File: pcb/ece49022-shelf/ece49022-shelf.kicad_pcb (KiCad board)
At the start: 4 copper layers, 44.2 x 53.6 mm, 69 parts, among them IC1 NAU7802, J1 USB_B_Micro, J2 Conn_01x16_Pin, J3 Conn_01x04_Pin, J4 SM03B-SRSS-TB, J6 Conn_01x02_Pin, J7 Conn_01x02_Pin, SW1 SW_Push, SW2 SW_Push, U2 TPS54202DDCT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

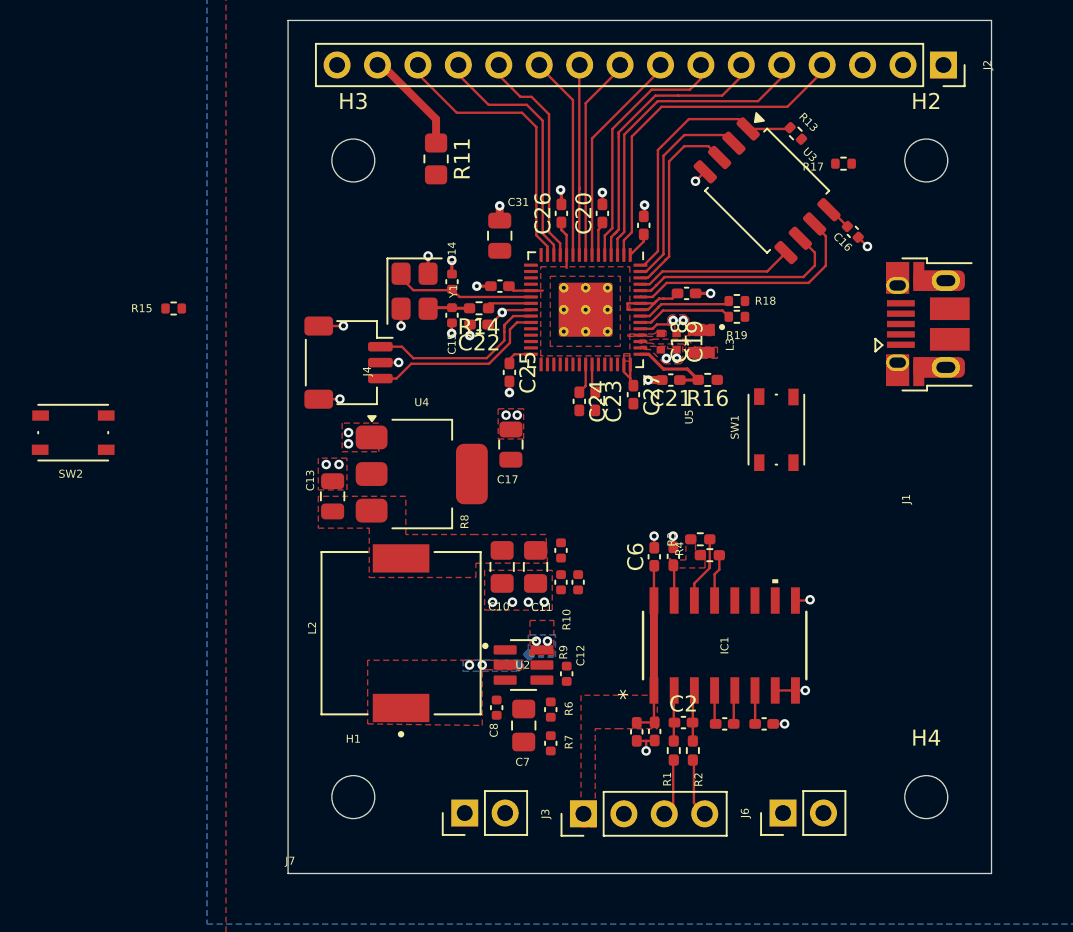
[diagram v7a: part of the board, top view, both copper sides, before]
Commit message: edited nau7802 schem and changed pins for layout reasons
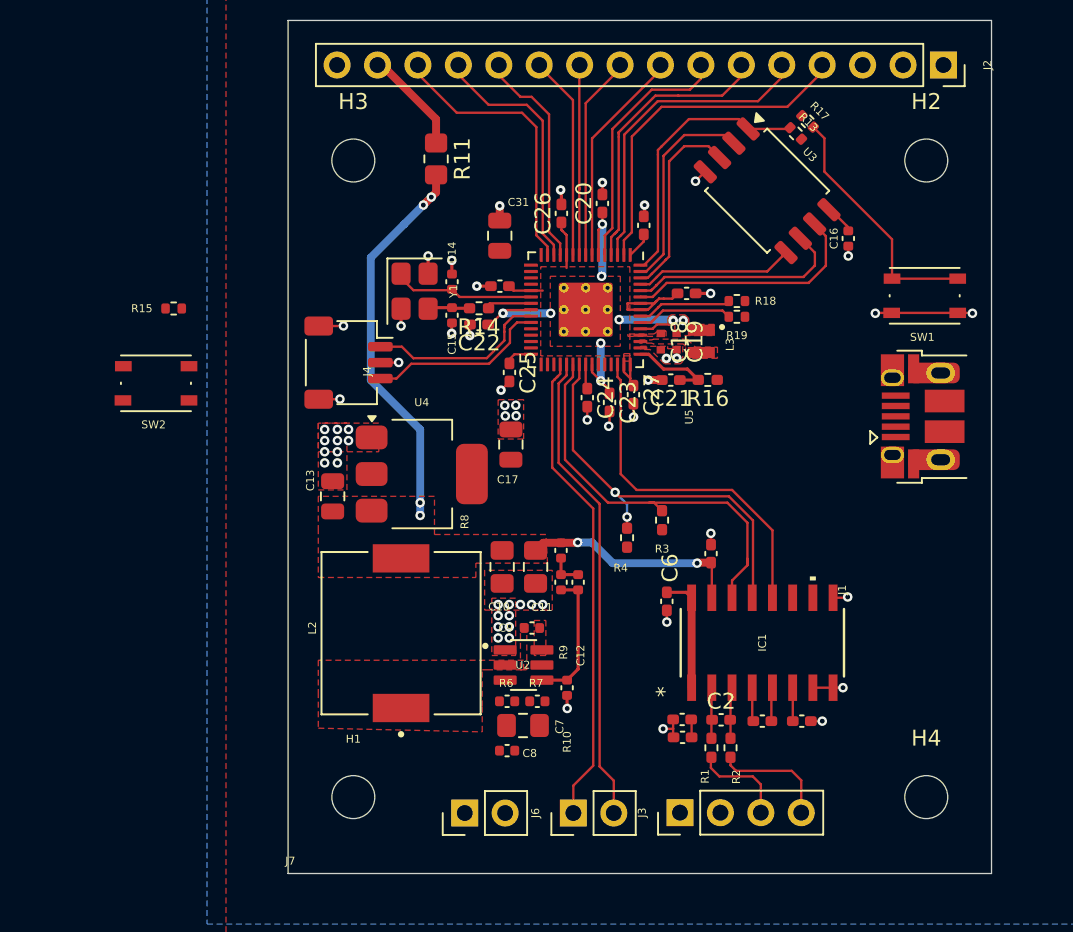
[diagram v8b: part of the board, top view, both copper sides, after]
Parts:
- C9: moved to F.Cu
- moved J6 13.2 mm to (171.8, 112.0)
- moved SW1 12.6 mm to (193.9, 79.5), turned to 180 degrees
- moved J3 6.07 mm to (178.5, 112.0)
- moved SW2 6.05 mm to (145.6, 85.0)
- moved J1 5.81 mm to (194.9, 87.1)
- moved R4 5.32 mm to (175.2, 94.7), turned to -90 degrees
- moved R17 3.49 mm to (186.5, 68.5), turned to -45 degrees
- moved C4 2.96 mm to (178.7, 106.1), turned to 180 degrees
- moved C6 2.91 mm to (177.7, 98.7), turned to -90 degrees
- moved R6 2.79 mm to (167.7, 105.0), turned to 0 degrees
- moved C8 2.78 mm to (167.7, 108.1), turned to 0 degrees
- moved R7 2.77 mm to (169.6, 105.0), turned to 0 degrees
- moved R3 2.68 mm to (177.4, 93.6), turned to -90 degrees
- moved C2 2.37 mm to (181.1, 106.1)
- moved C5 2.37 mm to (186.2, 106.2)
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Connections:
- R3 pad 2: +5V -> +3V3
- R4 pad 2: +5V -> +3V3
- U5 pad 15: /LOAD_CELL_I2C_SDA -> /RP2350A/GPIO11
- U5 pad 16: /LOAD_CELL_I2C_SCL -> /RP2350A/GPIO12
- U5 pad 18: /MAIN_MCU_I2C_SDA -> /RP2350A/GPIO14
- U5 pad 19: /MAIN_MCU_I2C_SCL -> /RP2350A/GPIO15
- U5 pad 28: /LOAD_CELL_DRDY -> /RP2350A/GPIO17
- U5 pad 34: /RP2350A/GPIO22 -> /MAIN_MCU_I2C_SDA
- U5 pad 35: /RP2350A/GPIO23 -> /MAIN_MCU_I2C_SCL
- U5 pad 36: /RP2350A/GPIO24 -> /LOAD_CELL_I2C_SDA
- U5 pad 37: /RP2350A/GPIO25 -> /LOAD_CELL_I2C_SCL
- U5 pad 43: /RP2350A/GPIO29_ADC3 -> /LOAD_CELL_DRDY
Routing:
- net +5V: track 2.23 -> 39.1 mm, vias 0 -> 6
- net /MAIN_MCU_I2C_SDA: track 0.00 -> 30.0 mm
- net /MAIN_MCU_I2C_SCL: track 0.00 -> 29.8 mm
- net /LOAD_CELL_I2C_SCL: track 2.97 -> 26.1 mm, vias 0 -> 2
- net /LOAD_CELL_DRDY: track 0.00 -> 22.2 mm
- net /LOAD_CELL_I2C_SDA: track 4.65 -> 25.8 mm
- net /RP2350A/~{USB_BOOT}: track 0.00 -> 15.7 mm
- net +1V1: track 9.32 -> 22.6 mm, vias 3 -> 9
- net GND: track 24.0 -> 33.2 mm, vias 36 -> 57
- net /Power/FB: track 0.00 -> 8.61 mm
- net /LOAD_CELL_N: track 3.69 -> 7.46 mm
- net AVDD: track 11.0 -> 8.55 mm
- net /LOAD_CELL_P: track 3.62 -> 6.02 mm
- net Net-(C12-Pad1): track 0.00 -> 2.11 mm
- net Net-(U2-SW): vias 2 -> 0
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- removed copper zone on F.Cu, net AVDD
- removed copper zone on B.Cu, net Net-(U2-BOOT)
- removed copper zone on B.Cu, net Net-(U2-SW)
